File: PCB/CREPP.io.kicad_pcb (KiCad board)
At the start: 2 copper layers, 101.9 x 139.4 mm, 104 parts, among them J1 Screw_Terminal_01x04, J10 Right_Connector, J11 Right_Connector, J12 Right_Connector, J13 Conn_02x04_Odd_Even, J14 OLED_SOCKET, J15 Conn_02x04_Odd_Even, J16 I2C_Selector, J17 Conn_02x04_Odd_Even, J18 Conn_02x04_Odd_Even, J19 Analog_Inputs, J2 HC-SR04_VIRTUAL, J20 GND_Analog, J21 +3.3V_Analog, J22 OLED_SOCKET_VIRTUAL, J23 HC-SR, J24 BME_VIRTUAL, J25 BME, J26 Addr_Selector, J27 SIG_HCSR04, J28 SIG_HC-05, J29 Conn_01x06_Socket, J3 Conn_02x04_Odd_Even, J30 Servo, J31 HC-05_VIRTUAL, J32 Power_Servo_Selector, J33 Screw_Terminal_01x02, J34 Sig_Servo, J35 SPI_Connector, J36 Power_Selector, J37 Sig_MOSFET, J4 Right_Connector, J5 Right_Connector, J6 Right_Connector, J7 Left_Connector, J8 Right_Connector, J9 Right_Connector, Q1 IRF520, SW1 SW_Left, SW2 SW_Up, SW3 SW_Right, SW4 SW_Down, T1 TestPoint, T4 TestPoint, U1 ADS1115IDGS, U14 DS1307+, U2 PC817, Y2 16MHz

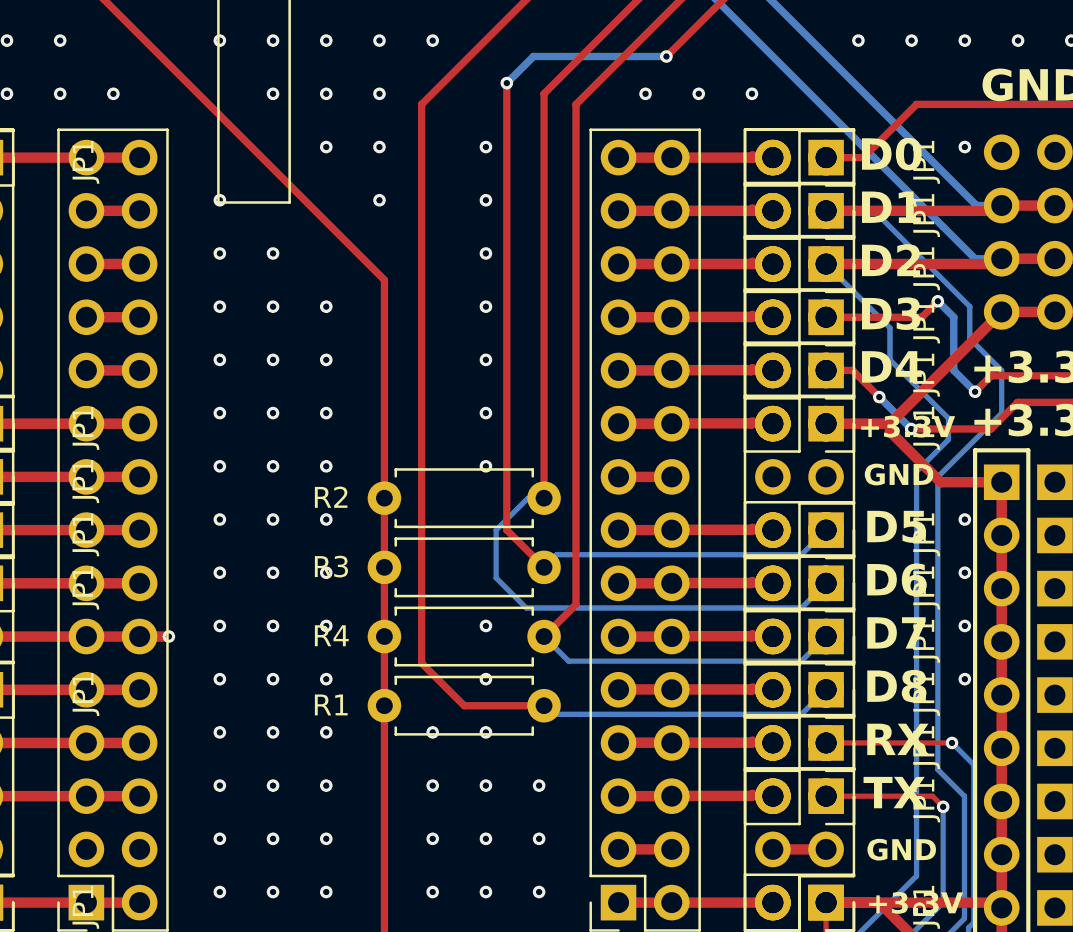
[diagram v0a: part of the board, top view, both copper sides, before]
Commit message: Update codes for LED and Potentiometer
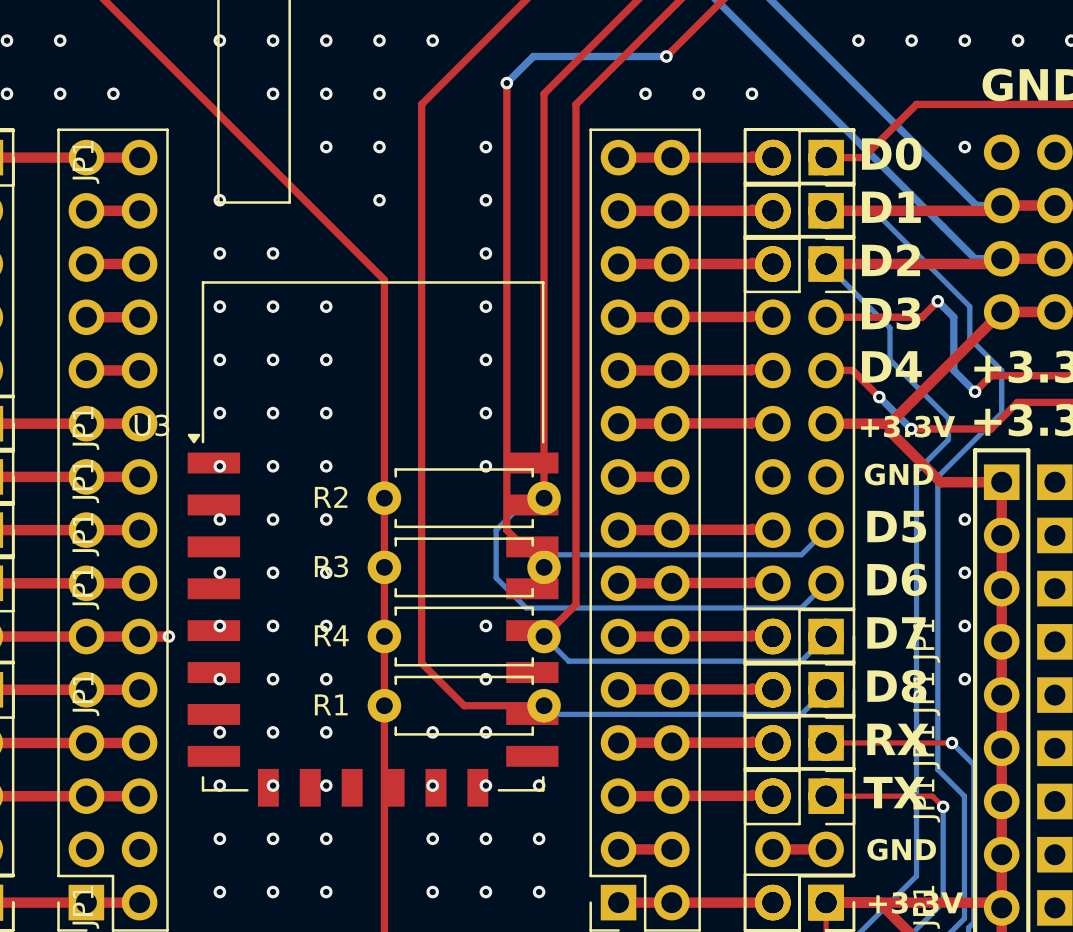
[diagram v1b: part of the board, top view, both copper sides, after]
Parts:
- removed the JP1 at (126.7, 75.2)
- removed the JP1 at (126.7, 93.0)
- removed the JP1 at (126.7, 82.8)
- removed the JP1 at (126.7, 87.9)
- removed the JP1 at (126.7, 95.5)
- removed the JP1 at (126.7, 85.3)
- added JP1: J2.54MM, Connector_PinHeader_2.54mm:PinHeader_2x01_P2.54mm_Vertical, F.Cu at (126.8, 75.2)
- added U3: ESP-12E_VIRTUAL, RF_Module:ESP-12E, F.Cu at (105.1, 93.3)
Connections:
- JP1 pad 1: (no net) -> unconnected-(JP1-A-Pad1) (x18)
- JP1 pad 2: (no net) -> unconnected-(JP1-B-Pad2) (x18)
